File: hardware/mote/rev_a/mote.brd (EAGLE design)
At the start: 79.4 x 89.5 mm, 135 parts, among them J1 TC2030-JLINK-L, Q1 CSD22206W, Q10 CSD22206W, Q11 CSD22206W, Q2 CSD22206W, Q6 CSD22206W, Q7 CSD22206W, Q8 CSD22206W, Q9 CSD22206W, U1 NRF52840, U10 MS5637-02BA03, U11 ADP5091, U12 NRF51822QF, U3 MAX17222, U4 AMN41121, U5 SI7021-A20-GM1, U6 ISL29125, U7 MAX44009, U8 LIS2DW12, U9 AB1815-T3, X1 7V-32.000MAHV-T, X2 ABS05-32.768KHZ-9-T, X3 ABS07-32.768KHZ-7-T, X5 16MHz, X6 ABS05-32.768KHZ-9-T

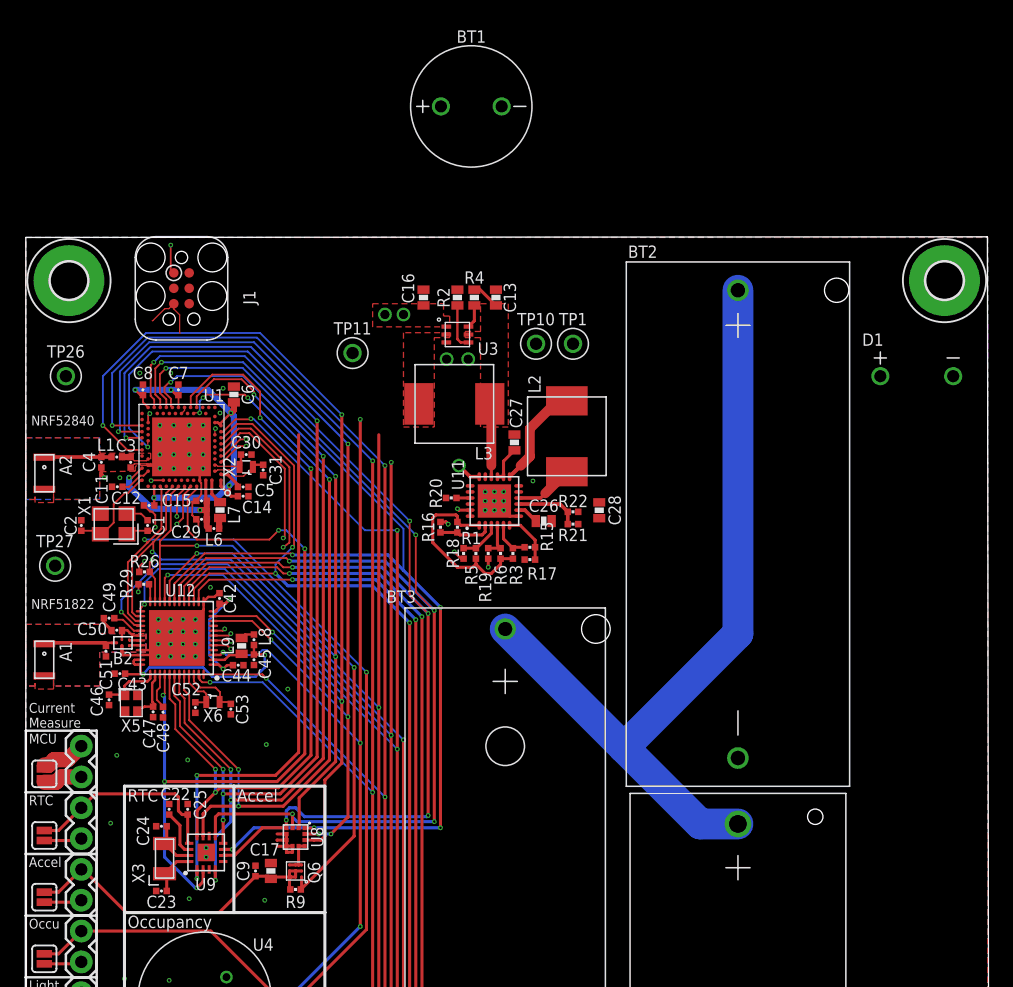
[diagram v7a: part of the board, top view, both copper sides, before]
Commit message: Power trace routed, few airwires left
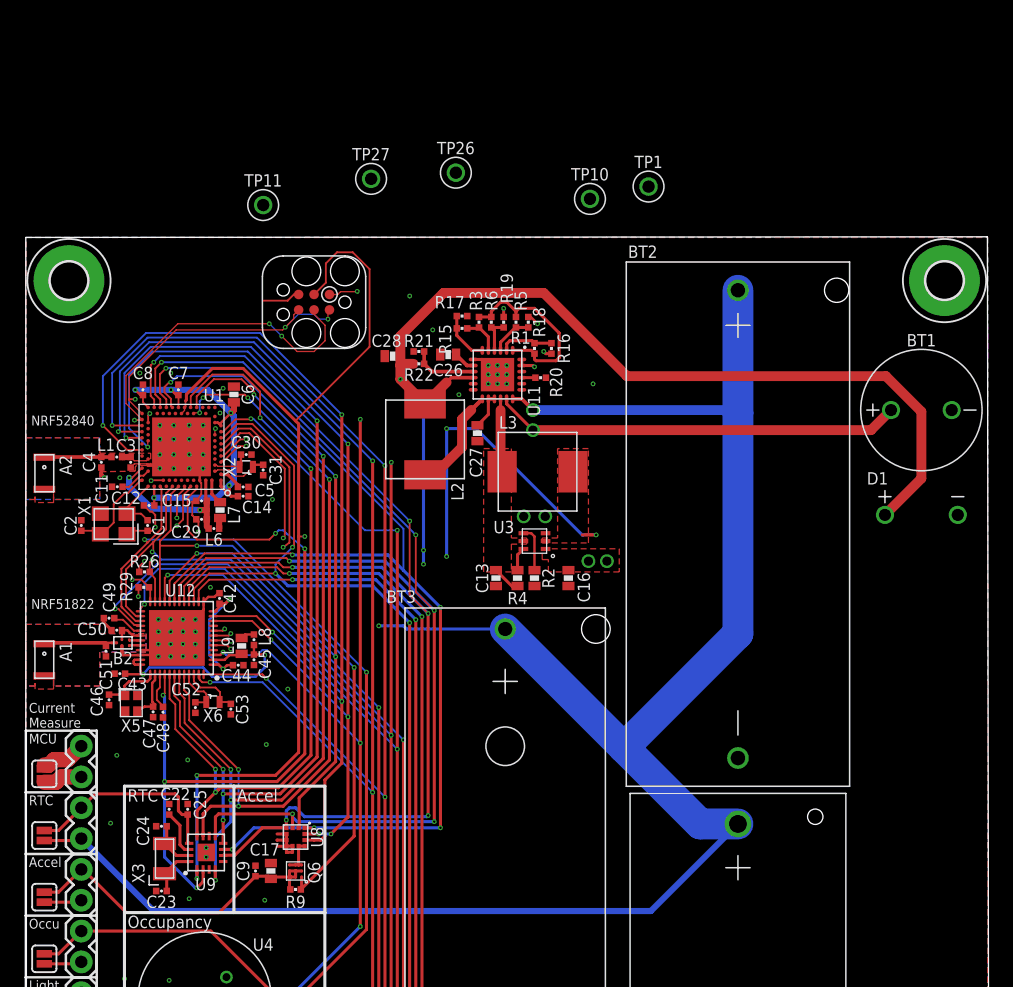
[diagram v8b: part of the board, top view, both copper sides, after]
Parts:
- moved BT1 44.7 mm to (73.8, 75.2)
- moved TP27 41.2 mm to (28.4, 94.2)
- moved TP26 36.2 mm to (35.4, 94.7)
- moved C16 26.0 mm to (44.7, 61.3), turned to 270 degrees
- moved R2 24.0 mm to (41.9, 61.3), turned to 90 degrees
- moved R4 23.4 mm to (40.5, 61.3), turned to 270 degrees
- moved C13 23.1 mm to (38.7, 61.3), turned to 270 degrees
- moved C28 21.2 mm to (30.2, 79.6), turned to 180 degrees
- moved R17 20.8 mm to (35.9, 82.9), turned to 180 degrees
- moved R18 19.8 mm to (41.4, 82.4), turned to 270 degrees
- moved R5 19.3 mm to (40.4, 82.4), turned to 90 degrees
- moved R3 19.3 mm to (37.3, 82.4), turned to 90 degrees
- moved R19 19.1 mm to (39.4, 82.4), turned to 270 degrees
- moved R21 19.1 mm to (32.4, 80.0), turned to 0 degrees
- moved R6 19.1 mm to (38.4, 82.4), turned to 90 degrees
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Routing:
- net VBAT: track 76.8 -> 201.3 mm, vias 3 -> 4
- net VSOL: track 9.96 -> 132.2 mm, vias 2 -> 5
- net VSEC: track 4.31 -> 102.4 mm, vias 2 -> 3
- net SW: track 3.62 -> 69.1 mm, vias 2 -> 5
- net !RST: track 46.3 -> 102.1 mm, vias 3 -> 4
- net SWDCLK: track 1.44 -> 47.0 mm, vias 0 -> 4
- net SWDIO: track 3.69 -> 46.4 mm, vias 1 -> 4
- net !LT_EN: track 111.9 -> 90.0 mm
- net VCC_JUMP: track 61.8 -> 71.6 mm
- net N$9: track 1.92 -> 4.89 mm
- net !PR_EN: track 93.9 -> 94.5 mm
- net GND: track 56.4 -> 56.5 mm, vias 73 -> 78
